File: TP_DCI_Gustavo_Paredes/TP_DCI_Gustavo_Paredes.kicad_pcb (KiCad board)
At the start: 2 copper layers, 30 parts, among them U101 LTC1485IS8PBF, U102 LTC1485IS8PBF, X701DB9F/101 DB9_Female, X702DB9M/101 DB9_Male

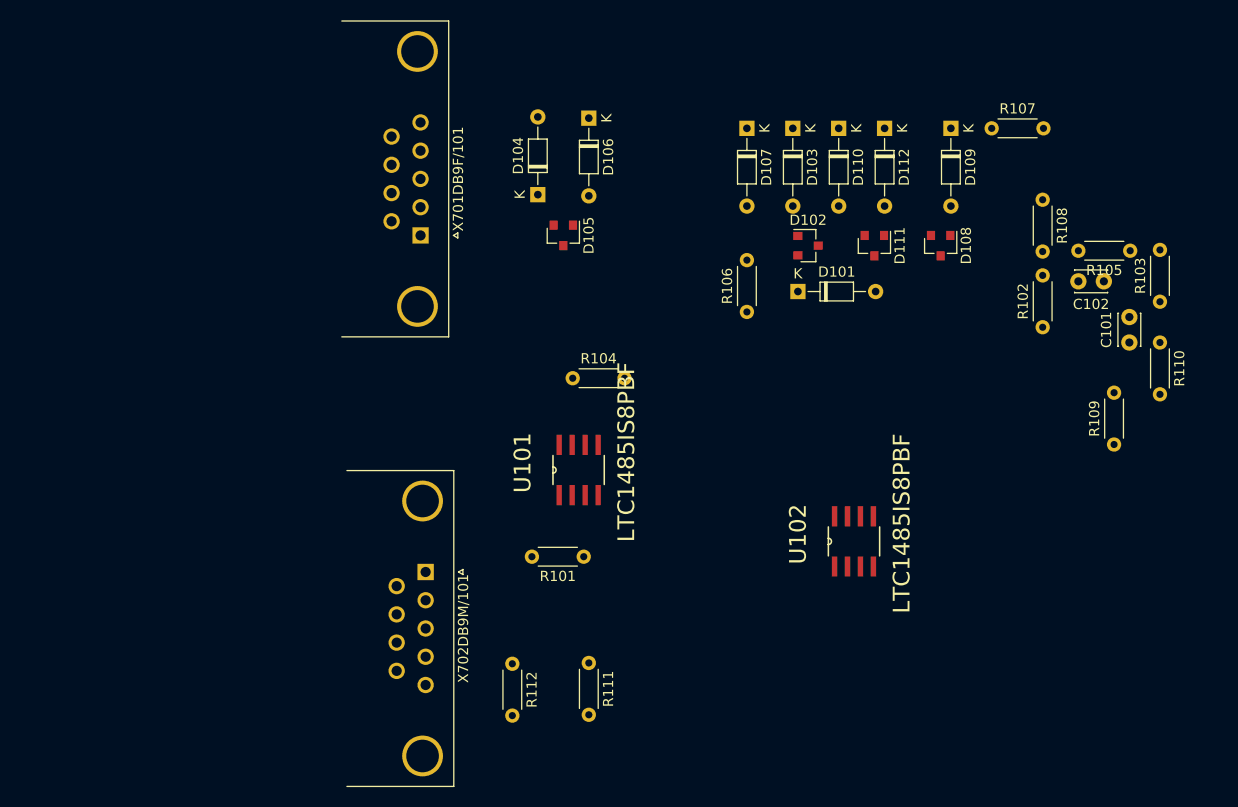
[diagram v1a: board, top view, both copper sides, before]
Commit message: Agregue Conector VCC
Agregue conector para 5V y GND. Ya esta hecha la distribucion basica de componentes en el PCB. Recargo la NETList.
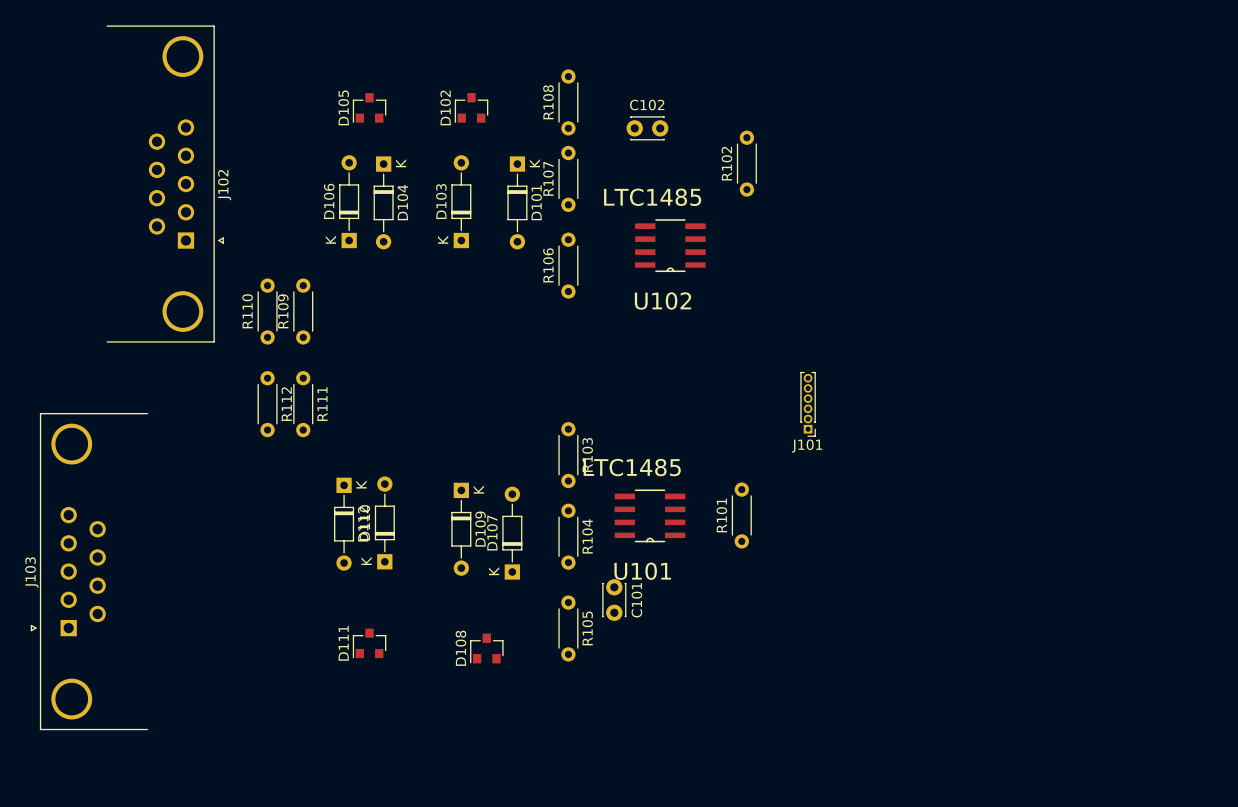
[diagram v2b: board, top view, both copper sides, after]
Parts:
- removed X701DB9F/101: DB9_Female, Connector_Dsub:DSUB-9_Female_Horizontal_P2.77x2.84mm_EdgePinOffset4.94mm_Housed_MountingHolesOffset7.48mm
- removed X702DB9M/101: DB9_Male, Connector_Dsub:DSUB-9_Male_Horizontal_P2.77x2.84mm_EdgePinOffset4.94mm_Housed_MountingHolesOffset7.48mm
- added J101: Conector, Connector_PinHeader_1.00mm:PinHeader_1x06_P1.00mm_Vertical, F.Cu at (139.5, 95.5)
- added J102: DB9 Hembra, Connector_Dsub:DSUB-9_Female_Horizontal_P2.77x2.84mm_EdgePinOffset4.94mm_Housed_MountingHolesOffset7.48mm, F.Cu at (78.5, 77.0)
- added J103: DB9 Macho, Connector_Dsub:DSUB-9_Male_Horizontal_P2.77x2.84mm_EdgePinOffset4.94mm_Housed_MountingHolesOffset7.48mm, F.Cu at (67.0, 115.0)
- D101, D104, D107, D110: value 4,7V -> BZX84C4V7
- D103, D106, D109, D112: value 8,2V -> BZX84C8V2
- R110, R111, R112: value 10R -> R10
- U101, U102: value LTC1485IS8PBF -> LTC1485
- moved R110 87.5 mm to (86.5, 86.5), turned to 90 degrees
- moved R109 80.2 mm to (90.0, 86.5)
- moved R105 65.0 mm to (116.0, 112.5), turned to 270 degrees
- moved D112 63.5 mm to (94.0, 101.0)
- moved D111 63.0 mm to (96.5, 116.5), turned to 90 degrees
- moved D110 61.5 mm to (98.0, 108.5), turned to 90 degrees
- moved D109 59.7 mm to (105.5, 101.5)
- moved D108 59.5 mm to (108.0, 117.0), turned to 90 degrees
- moved R103 59.3 mm to (116.0, 95.5), turned to 270 degrees
- moved C101 55.9 mm to (120.5, 111.0), turned to 270 degrees
- moved D107 49.2 mm to (110.5, 109.5), turned to 90 degrees
- moved C102 48.4 mm to (122.5, 66.0), turned to 0 degrees
- moved R108 47.0 mm to (116.0, 66.0), turned to 90 degrees
- moved R107 42.2 mm to (116.0, 73.5), turned to 90 degrees
- moved R111 39.5 mm to (90.0, 90.5)
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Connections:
- D101 pad 2: /A_Data_N -> Net-(D101-Pad2)
- D103 pad 1: /A_Data_N -> Net-(D101-Pad2)
- D104 pad 2: /A_Data_P -> Net-(D104-Pad2)
- D106 pad 1: /A_Data_P -> Net-(D104-Pad2)
- D107 pad 2: /B_Data_N -> Net-(D107-Pad2)
- D109 pad 1: /B_Data_N -> Net-(D107-Pad2)
- D110 pad 2: /B_Data_P -> Net-(D110-Pad2)
- D112 pad 1: /B_Data_P -> Net-(D110-Pad2)
- R103 pad 2: /A_Data_N -> Net-(D107-Pad2)
- R104 pad 1: /A_Data_N -> Net-(D107-Pad2)
- R104 pad 2: /A_Data_N -> Net-(D110-Pad2)
- R105 pad 1: /A_Data_N -> Net-(D110-Pad2)
- R106 pad 2: /B_Data_N -> Net-(D101-Pad2)
- R107 pad 1: /B_Data_N -> Net-(D101-Pad2)
- R111 pad 1: Net-(R111-Pad1) -> +5V
- R111 pad 2: +5V -> Net-(J103-Pad8)
- R112 pad 1: Net-(R111-Pad1) -> +5V
- R112 pad 2: +5V -> Net-(J103-Pad8)
- U101 pad 6: /A_Data_N -> Net-(D107-Pad2)
- U101 pad 7: /A_Data_N -> Net-(D110-Pad2)
- U102 pad 6: /B_Data_N -> Net-(D101-Pad2)
- U102 pad 7: /B_Data_P -> Net-(D104-Pad2)

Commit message: Correcciones Esquematico V3
Se realizaron las correcciones menores que el Docente indico. Se actualizo huella y 3D del LTC1485 y los dos DB9.
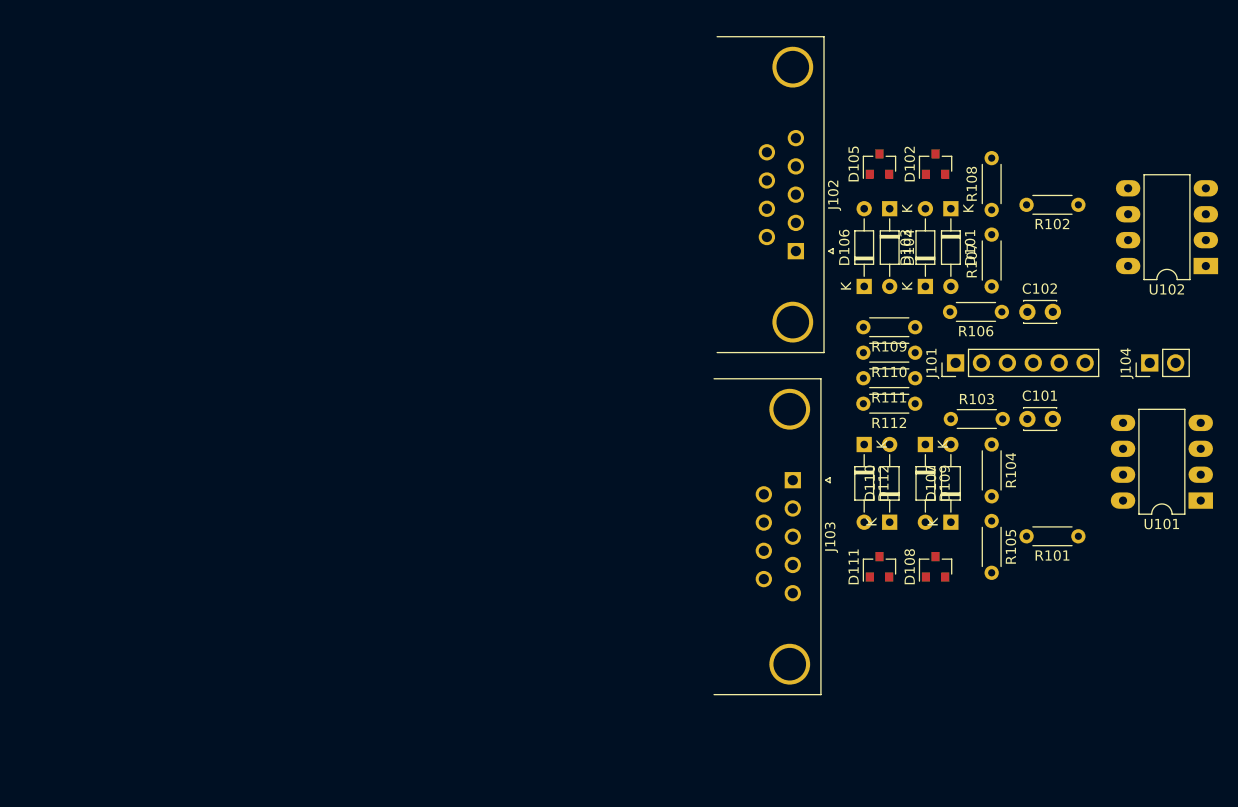
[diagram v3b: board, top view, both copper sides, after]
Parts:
- added J104: Conector +5V, Connector_PinHeader_2.54mm:PinHeader_1x02_P2.54mm_Vertical, F.Cu at (173.0, 89.0)
- J101: footprint Connector_PinHeader_1.00mm:PinHeader_1x06_P1.00mm_Vertical -> Connector_PinHeader_2.54mm:PinHeader_1x06_P2.54mm_Vertical
- R110, R111, R112: value R10 -> 10R
- U101, U102: footprint LTC1485IS8PBF:SOIC127P600X175-8N -> Package_DIP:DIP-8_W7.62mm_LongPads
- moved J103 72.5 mm to (138.0, 100.5), turned to 270 degrees
- moved R112 63.5 mm to (150.0, 93.0), turned to 180 degrees
- moved R110 63.5 mm to (150.0, 88.0), turned to 180 degrees
- moved R109 60.0 mm to (150.0, 85.5), turned to 180 degrees
- moved R111 60.0 mm to (150.0, 90.5), turned to 180 degrees
- moved J102 59.8 mm to (138.3, 78.0)
- moved U101 54.0 mm to (178.0, 102.5)
- moved U102 52.5 mm to (178.5, 79.5)
- moved D112 51.2 mm to (145.0, 97.0)
- moved D106 50.7 mm to (145.0, 81.5)
- moved D111 50.6 mm to (146.5, 109.0)
- moved D105 50.3 mm to (146.5, 69.5)
- moved D104 49.8 mm to (147.5, 73.9)
- moved D110 49.7 mm to (147.5, 104.6)
- moved D102 45.8 mm to (152.0, 69.5)
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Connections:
- net Net-(D101-Pad2) renamed /B_Data_N
- net Net-(D104-Pad2) renamed /B_Data_P
- net Net-(D107-Pad2) renamed /A_Data_N
- net Net-(D110-Pad2) renamed /A_Data_P

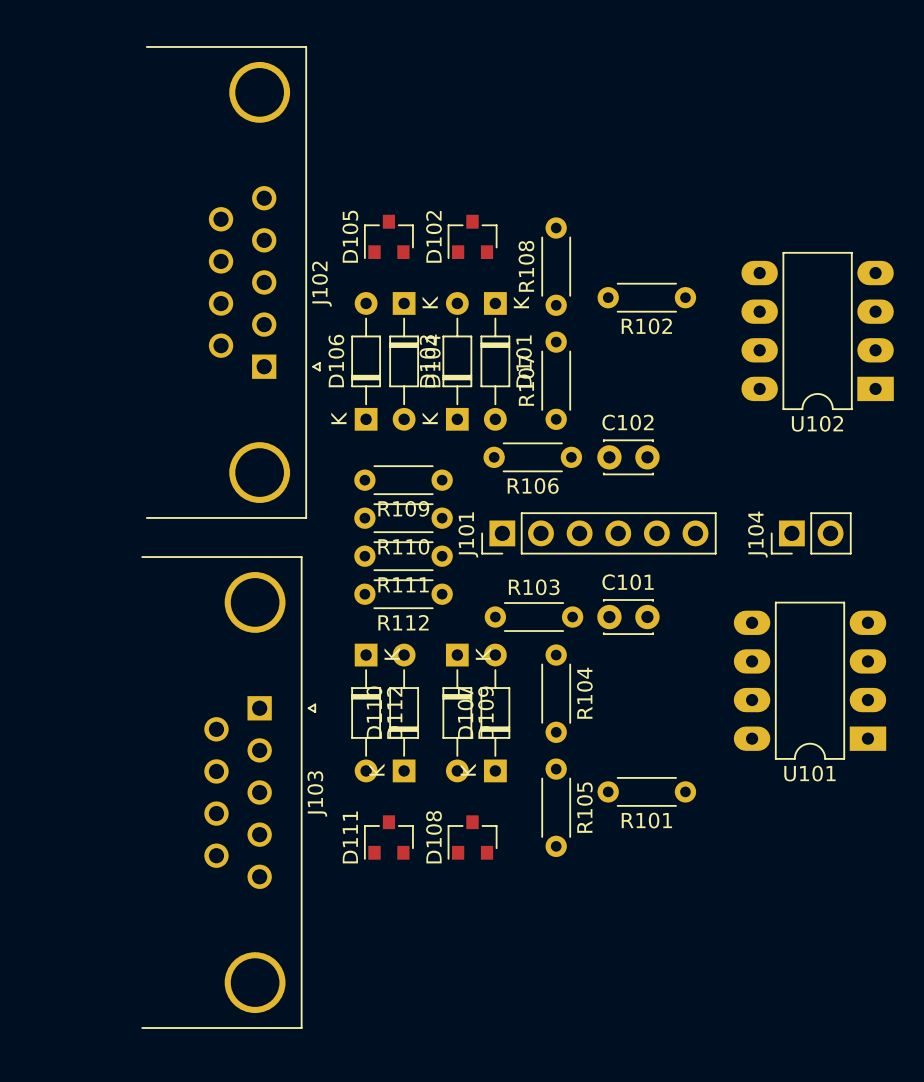
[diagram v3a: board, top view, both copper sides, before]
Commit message: Se ruteo el PCB
Primer intento de ruteo.
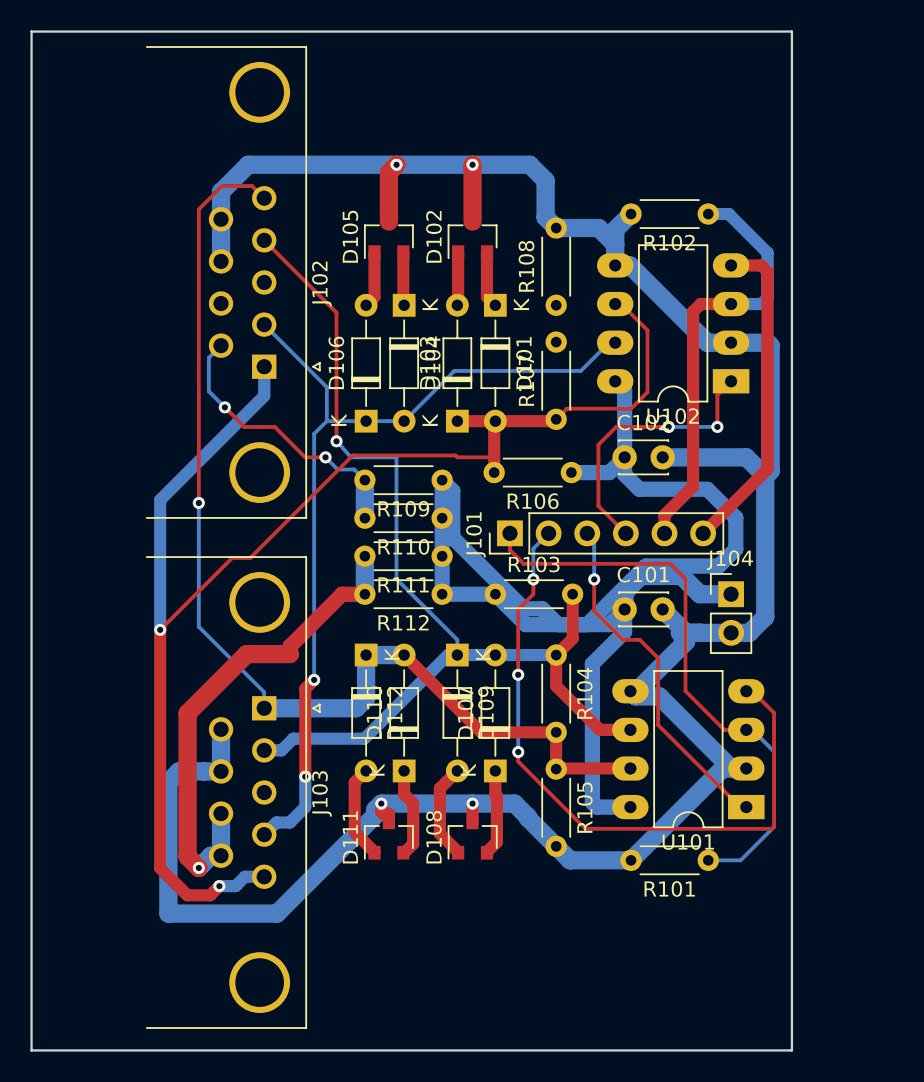
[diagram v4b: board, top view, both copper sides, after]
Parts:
- moved U102 9.51 mm to (169.0, 79.0)
- moved U101 9.18 mm to (170.0, 107.0)
- moved R102 5.70 mm to (167.5, 68.0)
- moved J104 5.66 mm to (169.0, 93.0), turned to 0 degrees
- moved R101 4.74 mm to (167.5, 110.5)
- moved R103 1.50 mm to (153.5, 93.0)
- moved C101 1.12 mm to (162.0, 94.0)
- moved C102 1.00 mm to (162.0, 84.0)
- moved R106 1.00 mm to (158.5, 85.0)
- moved J101 0.50 mm to (154.5, 89.0)
- moved J103 0.30 mm to (138.3, 100.5)
- moved D101 0.12 mm to (153.5, 74.0)
- moved D103 0.12 mm to (151.0, 81.6)
- moved D104 0.12 mm to (147.5, 74.0)
- moved D106 0.12 mm to (145.0, 81.6)
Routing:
- net GNDD: track 0.00 -> 171.9 mm, vias 0 -> 4
- net /B_Data_N: track 0.00 -> 95.3 mm, vias 0 -> 2
- net +5V: track 0.00 -> 94.0 mm
- net /A_Data_P: track 0.00 -> 71.6 mm, vias 0 -> 1
- net /A_Data_N: track 0.00 -> 68.7 mm, vias 0 -> 1
- net /B_Data_P: track 0.00 -> 58.6 mm, vias 0 -> 2
- net /LINE_A_D0: track 0.00 -> 44.5 mm, vias 0 -> 3
- net /LINE_A_SF: track 0.00 -> 38.5 mm
- net Net-(J103-Pad8): track 0.00 -> 32.7 mm, vias 0 -> 1
- net /LINE_B_SF: track 0.00 -> 28.6 mm
- net /LINE_A_D1: track 0.00 -> 23.2 mm, vias 0 -> 1
- net /LINE_B_D0: track 0.00 -> 21.5 mm
- net Net-(J102-Pad6): track 0.00 -> 19.5 mm, vias 0 -> 2
- net /LINE_B_D1: track 0.00 -> 18.3 mm, vias 0 -> 2
- net Net-(D108-Pad1): track 0.00 -> 6.35 mm
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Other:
- board outline added: 50 x 67 mm
- net class Default: clearance 0.2 -> 0.5
- rule trace_clearance: 0.2 -> 0.5

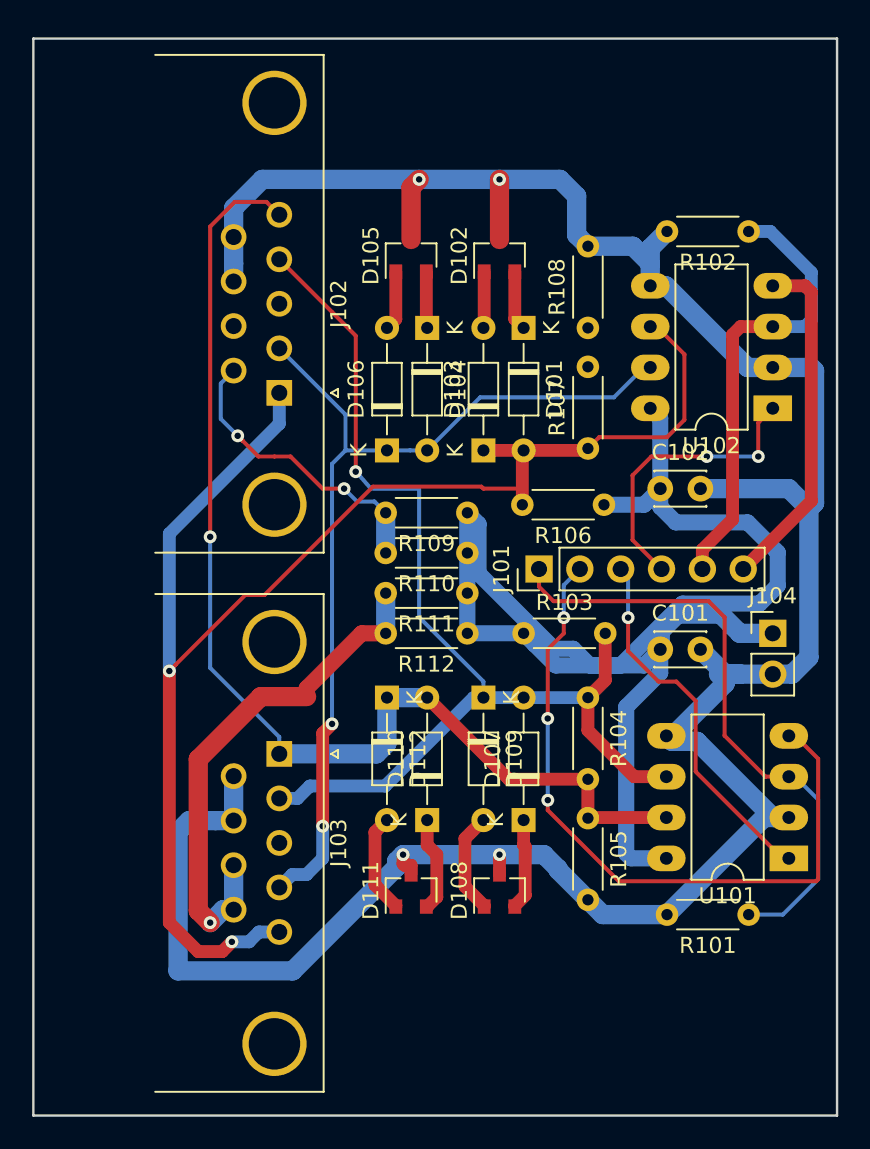
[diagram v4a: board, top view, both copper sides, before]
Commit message: PCB V1
Se termina V1 del PCB a la espera de las correcciones.
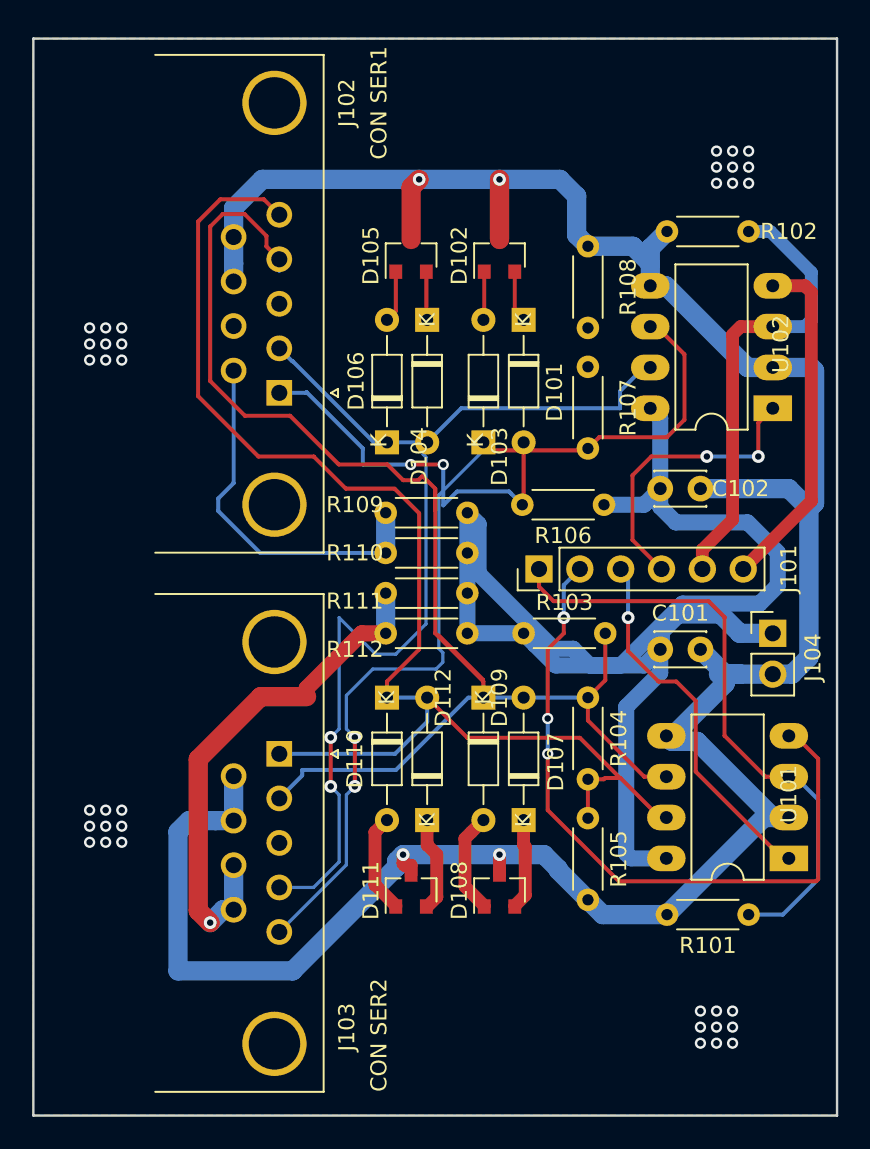
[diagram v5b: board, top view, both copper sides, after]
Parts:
- moved D101 0.50 mm to (153.5, 73.5)
- moved D103 0.50 mm to (151.0, 81.1)
- moved D104 0.50 mm to (147.5, 73.5)
- moved D106 0.50 mm to (145.0, 81.1)
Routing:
- net /A_Data_N: track 68.7 -> 88.4 mm, vias 1 -> 0
- net /B_Data_N: track 95.3 -> 82.6 mm, vias 2 -> 4
- net /A_Data_P: track 71.6 -> 82.4 mm, vias 1 -> 0
- net /B_Data_P: track 58.6 -> 66.4 mm
- net Net-(J102-Pad6): track 19.5 -> 23.1 mm, vias 2 -> 0
- net Net-(D105-Pad1): track 3.73 -> 3.23 mm
- net Net-(D104-Pad1): track 3.52 -> 3.02 mm
- net Net-(D102-Pad1): track 3.52 -> 3.02 mm
- net Net-(D101-Pad1): track 3.73 -> 3.23 mm
- net GNDD: vias 4 -> 40
- added copper zone on B.Cu, net GNDD
- added copper zone on F.Cu, net GNDD
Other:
- net class Default: via_dia 0.8 -> 0.7
- board text added: "Ancho de pista (min) = 0,250 mm Via (min) = 0,7 mm Agujero de via (min) = 0,4 mm"
- board text added: "CESE UBA - DCI - 7ma Cohorte Gustavo F. Paredes Delaloye"
- board text added: "CON SER1"
- board text added: "CON SER2"
- board text added: "Estándares de fabricación de Mayer Diámetro de agujero 16 (0,40 mm) Diámetro de pad o vía 28 (0,70 mm) Ancho de traza 5 (0,125 mm) Separación entre trazas 5 (0,125 mm) Separación entre traza y pad/vía 5 (0,125 mm) Distancia de cobre a borde 12 (0,30 mm) Altura - trazo de letras 30 - 5"
- board text added: "INDUSTRIA ARGENTINA"
- board text added: "KP995 RS485 PORT"
